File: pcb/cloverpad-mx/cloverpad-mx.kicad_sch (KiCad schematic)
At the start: 42 parts, among them J1 USB_C_Receptacle_USB2.0, SW1 SW_Push, SW2 SW_Push, U1 SRV05-4, U2 XC6206P332MR, U8 RP2040, U9 W25Q16JVSSIQ, Y1 12MHz

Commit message: fix: port pcb shape changes to cloverpad mx
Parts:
- H1, H2, H3, H4: footprint MountingHole:MountingHole_3.5mm_Pad -> MountingHole:MountingHole_2.2mm_M2_Pad

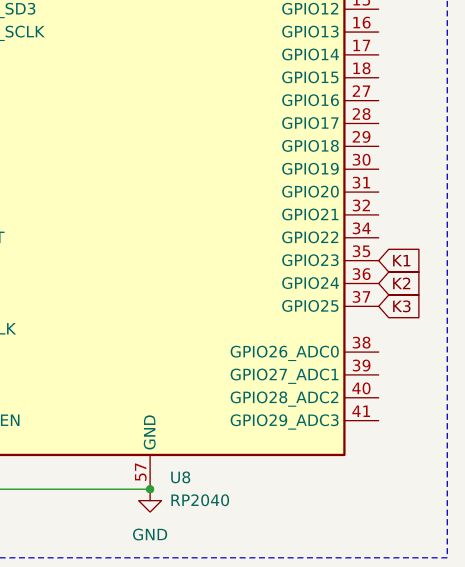
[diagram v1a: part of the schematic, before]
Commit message: fix: swap positions of MX1 and MX3 on cloverpad mx
makes more sense as when viewed from the front, MX1 is the leftmost switch.
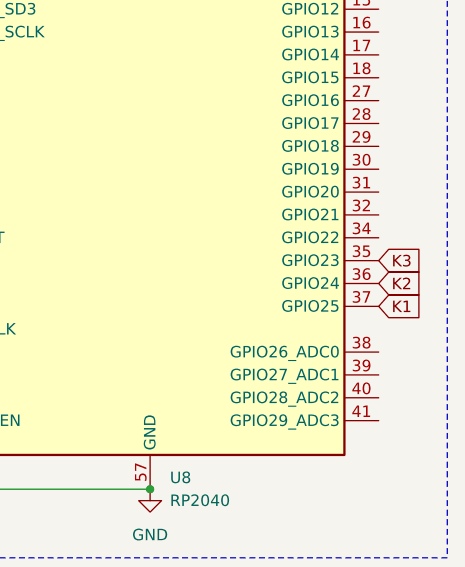
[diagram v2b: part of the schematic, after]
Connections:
- net K1: now also U8.37 (GPIO25); no longer U8.35 (GPIO23)
- net K3: now also U8.35 (GPIO23); no longer U8.37 (GPIO25)
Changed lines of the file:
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@@
     )
   )
-  (global_label "K1" (shape input) (at 261.62 111.76 0) (fields_autoplaced)
+  (global_label "K1" (shape input) (at 261.62 116.84 0) (fields_autoplaced)
     (effects (font (size 1.27 1.27)) (justify left))
-    (property "Intersheetrefs" "${INTERSHEET_REFS}" (at 267.0847 111.76 0)
+    (property "Intersheetrefs" "${INTERSHEET_REFS}" (at 267.0847 116.84 0)
       (effects (font (size 1.27 1.27)) (justify left) hide)
     )
@@
     )
   )
-  (global_label "K3" (shape input) (at 261.62 116.84 0) (fields_autoplaced)
+  (global_label "K3" (shape input) (at 261.62 111.76 0) (fields_autoplaced)
     (effects (font (size 1.27 1.27)) (justify left))
-    (property "Intersheetrefs" "${INTERSHEET_REFS}" (at 267.0847 116.84 0)
+    (property "Intersheetrefs" "${INTERSHEET_REFS}" (at 267.0847 111.76 0)
       (effects (font (size 1.27 1.27)) (justify left) hide)
     )
